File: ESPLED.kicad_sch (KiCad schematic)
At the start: 32 parts, among them J1 PWM-1, J2 PWM-2, J3 PWM-3, J4 PWM-4, J5 GND, J6 12V, J7 5V-Stb, Q1 AO D403, Q2 BSS138, Q3 BSS138, Q4 AO D403, Q5 AO D403, Q6 AO D403, U1 mini_esp32, X1 234-503, X2 234-503

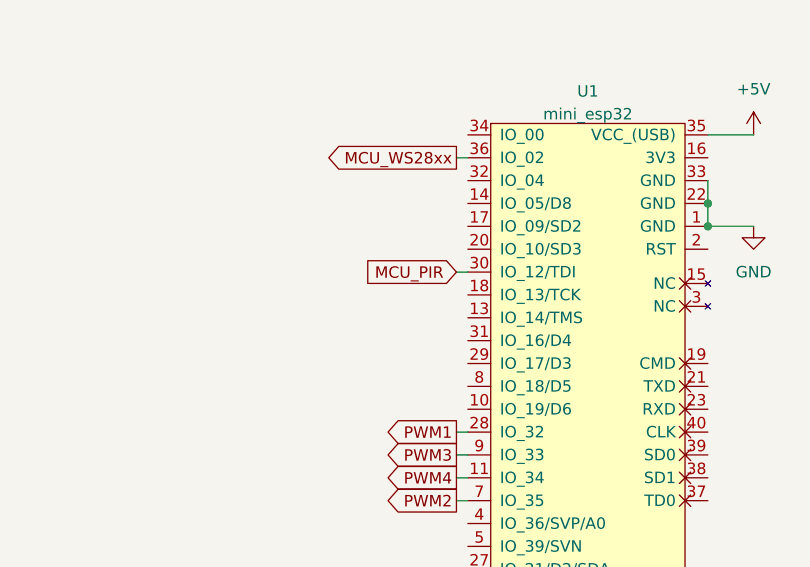
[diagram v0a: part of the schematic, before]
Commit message: Changed PIR from IO12 (strapping pin) to IO13
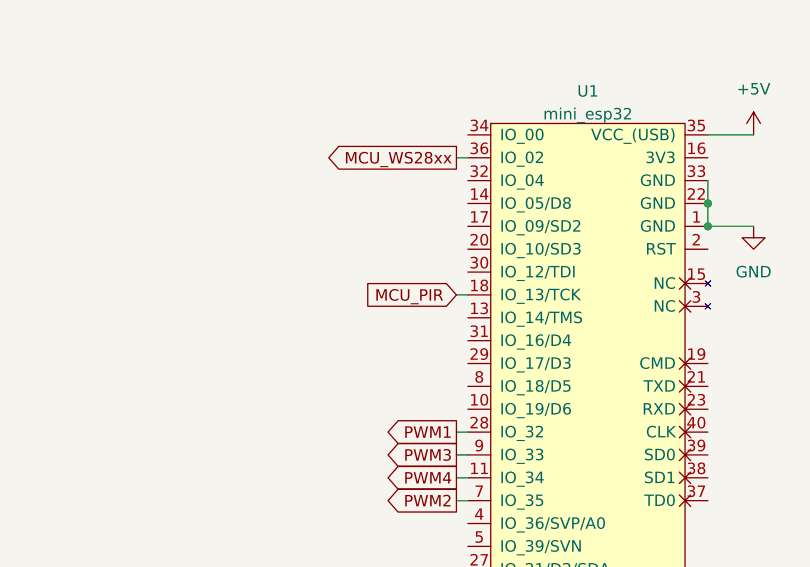
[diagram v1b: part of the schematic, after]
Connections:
- net MCU_PIR: now also U1.18 (IO_13/TCK); no longer U1.30 (IO_12/TDI)
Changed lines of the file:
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@@
-	(wire
-		(pts
-			(xy 87.63 80.01) (xy 88.9 80.01)
-		)
-		(stroke
-			(width 0)
-			(type default)
-		)
-	)
 	(wire
 		(pts
@@
 		(pts
 			(xy 223.52 49.53) (xy 224.79 49.53)
+		)
+		(stroke
+			(width 0)
+			(type default)
+		)
+	)
+	(wire
+		(pts
+			(xy 87.63 82.55) (xy 88.9 82.55)
 		)
 		(stroke
@@
 	(global_label "MCU_PIR"
 		(shape input)
-		(at 87.63 80.01 180)
-		(fields_autoplaced yes)
-		(effects
-			(font
-				(size 1.27 1.27)
-			)
-			(justify right)
-		)
-		(property "Intersheetrefs" "${INTERSHEET_REFS}"
-			(at 76.4805 80.01 0)
-			(effects
-				(font
+		(at 87.63 82.55 180)
+		(fields_autoplaced yes)
+		(effects
+			(font
+				(size 1.27 1.27)
+			)
+			(justify right)
+		)
+		(property "Intersheetrefs" "${INTERSHEET_REFS}"
+			(at 76.4805 82.55 0)
+			(effects
+				(font
